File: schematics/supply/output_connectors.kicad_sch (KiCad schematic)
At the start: 26 parts, among them J14 banana jack + fuse 15A, J15 banana jack + fuse 15A, J16 Conn_02x04_Odd_Even, J17 jst xh angle, J18 jst xh angle, Q10 IRLML0030, Q10 IRLML5203, U6 INA3221

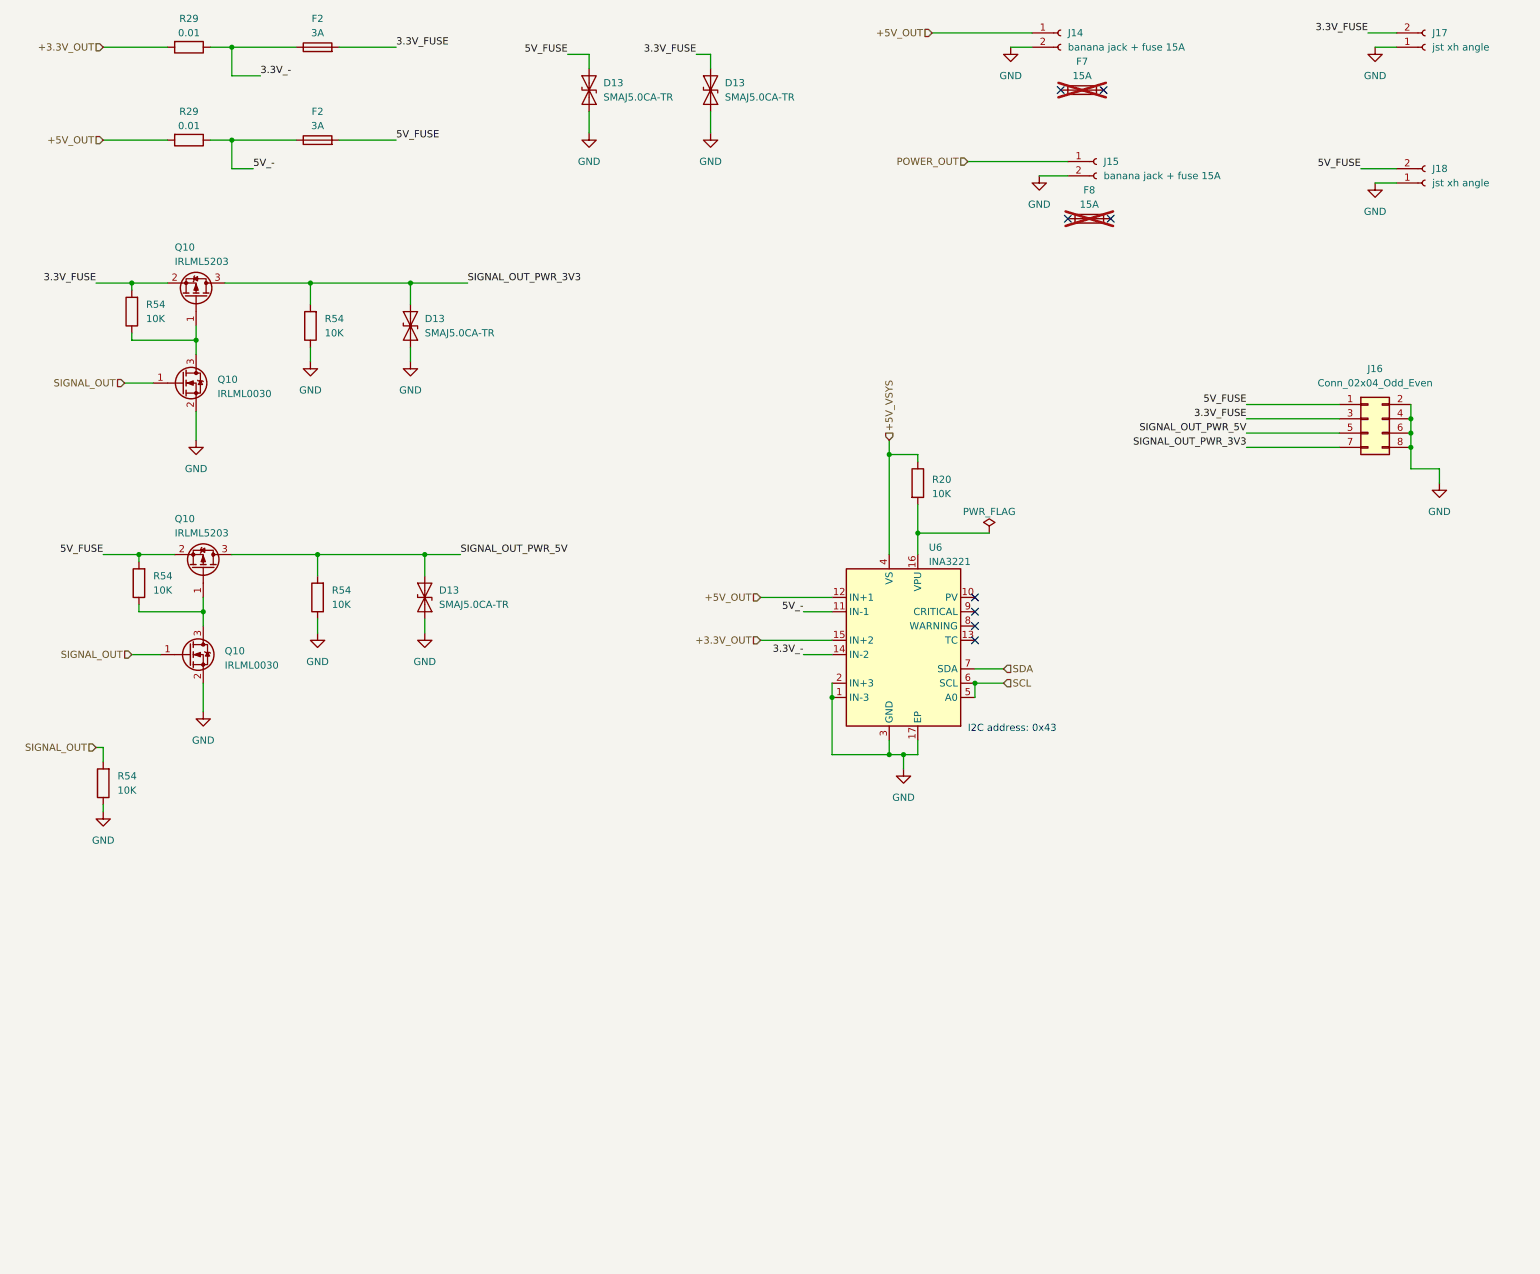
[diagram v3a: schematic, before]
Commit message: Added Li-Ion charger port
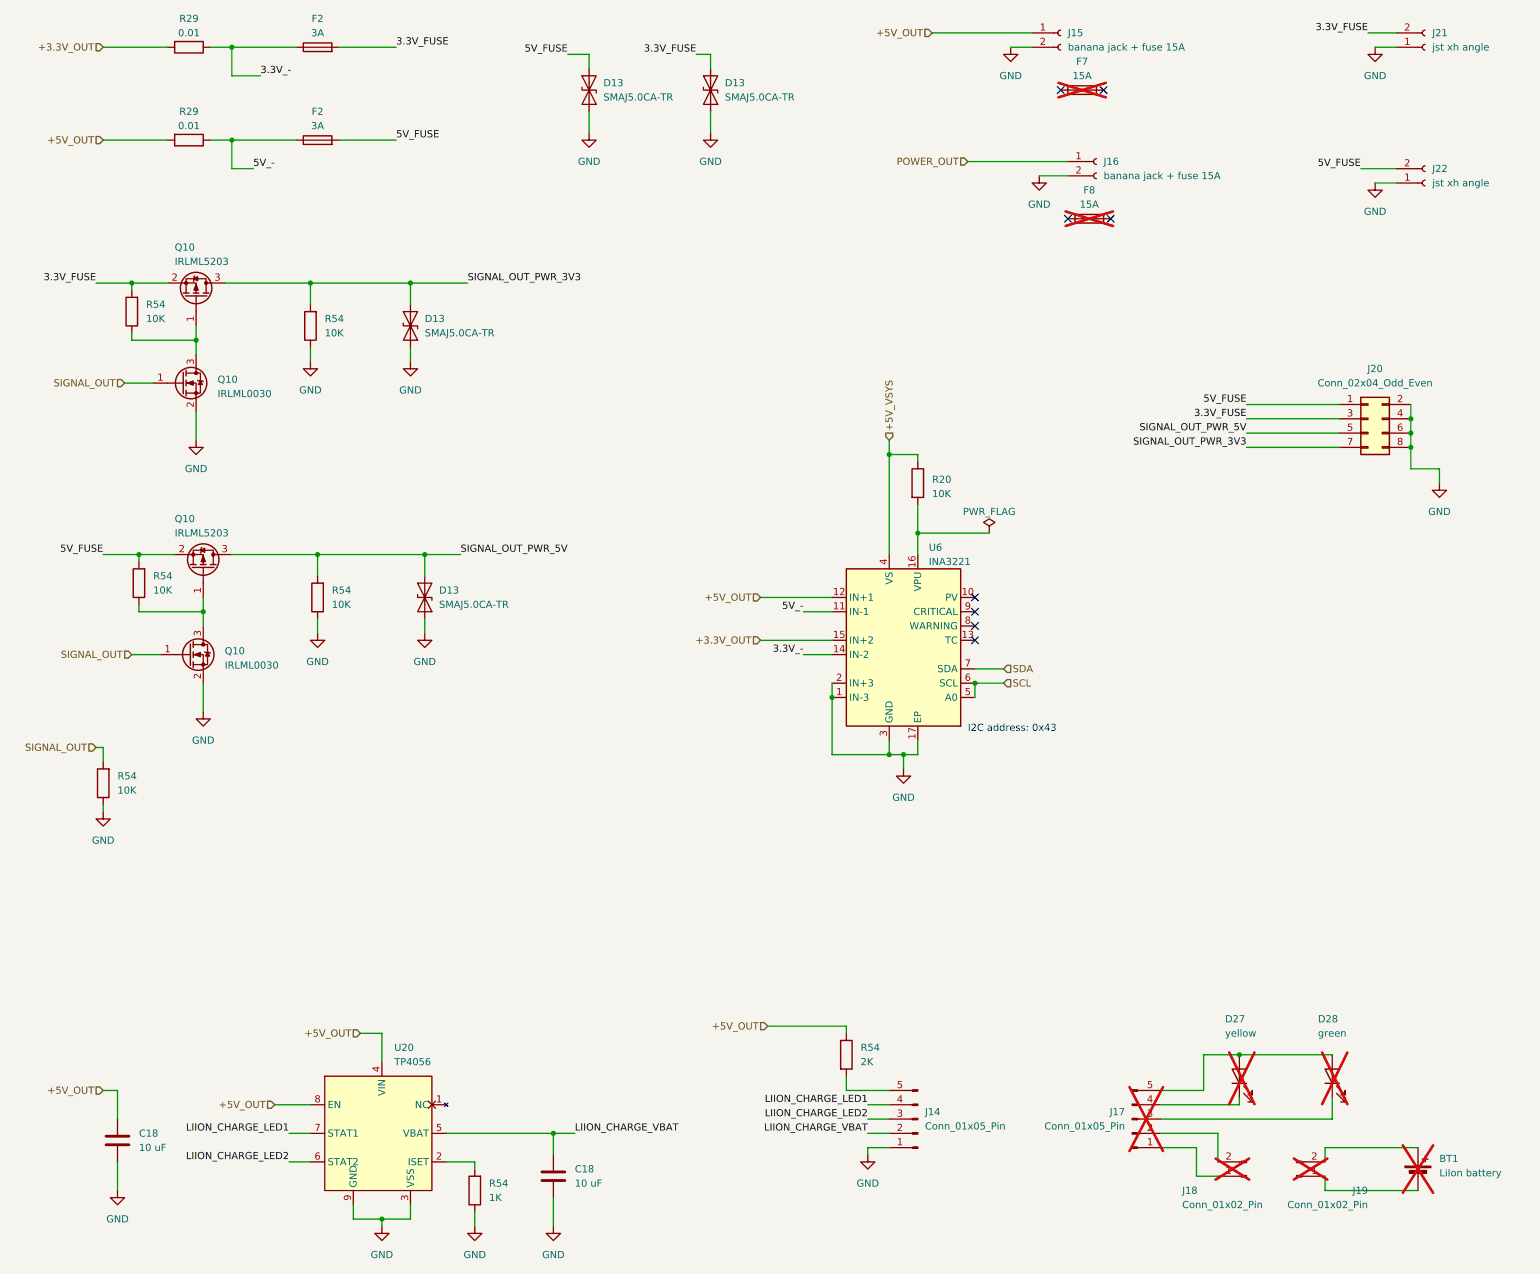
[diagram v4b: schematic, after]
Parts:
- added BT1: LiIon battery, symbol Device:Battery_Cell
- added C18 (x2): 10 uF, Capacitor_SMD:C_0603_1608Metric, symbol Device:C
- added D27: yellow, symbol Device:LED
- added D28: green, symbol Device:LED
- added J14: Conn_01x05_Pin, Connector_JST:JST_XH_B5B-XH-A_1x05_P2.50mm_Vertical, symbol Connector:Conn_01x05_Pin
- added J17: Conn_01x05_Pin, symbol Connector:Conn_01x05_Pin
- added J18: Conn_01x02_Pin, Connector_JST:JST_XH_B2B-XH-A_1x02_P2.50mm_Vertical, symbol Connector:Conn_01x02_Pin
- added J19: Conn_01x02_Pin, symbol Connector:Conn_01x02_Pin
- added R54: 2K, Resistor_SMD:R_0805_2012Metric, symbol Device:R
- added R54: 1K, Resistor_SMD:R_0805_2012Metric, symbol Device:R
- added U20: TP4056, Library:SOP127P600X175-9N, symbol My_Library:TP4056
- renumbered J14 to J15, J15 to J16, J16 to J20, J17 to J21, J18 to J22
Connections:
- net +5V_OUT: now also C18.2, R54.1, U20.4 (VIN), U20.8 (EN)
- net GND: now also C18.1, C18.1, J14.1 (Pin_1), R54.1, U20.3 (VSS), U20.9 (GND)
- new net: BT1.2 (-), J19.1 (Pin_1)
- new net: BT1.1 (+), J19.2 (Pin_2)
- new net: D28.1 (K), J17.3 (Pin_3)
- new net: D27.2 (A), D28.2 (A), J17.5 (Pin_5)
- new net: D27.1 (K), J17.4 (Pin_4)
- new net: J14.5 (Pin_5), R54.2
- new net: R54.2, U20.2 (ISET)
- new net: J17.1 (Pin_1), J18.1 (Pin_1)
- new net: J17.2 (Pin_2), J18.2 (Pin_2)
- new net LIION_CHARGE_LED1: J14.4 (Pin_4), U20.7 (STAT1)
- new net LIION_CHARGE_LED2: J14.3 (Pin_3), U20.6 (STAT2)
- new net LIION_CHARGE_VBAT: C18.2, J14.2 (Pin_2), U20.5 (VBAT)
